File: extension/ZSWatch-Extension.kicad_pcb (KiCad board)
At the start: 4 copper layers, 18 x 18 mm, 37 parts, among them IC501 MAX32664, IC502 LIS2DS12, IC503 MAX86141, IC601 DA7212-01UM2, X701 MB2, X702 MB1, Y501 32kHz

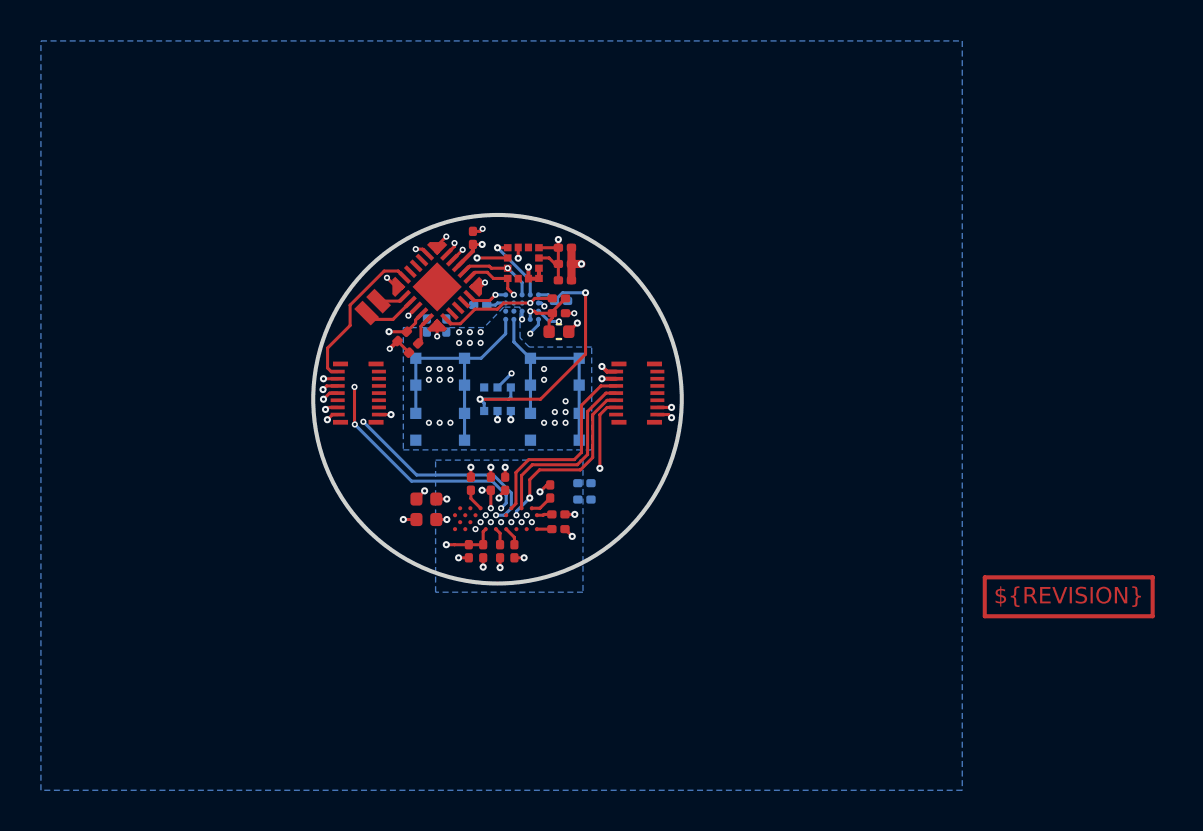
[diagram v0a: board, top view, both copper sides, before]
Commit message: Reduce radius to 8.4 mm
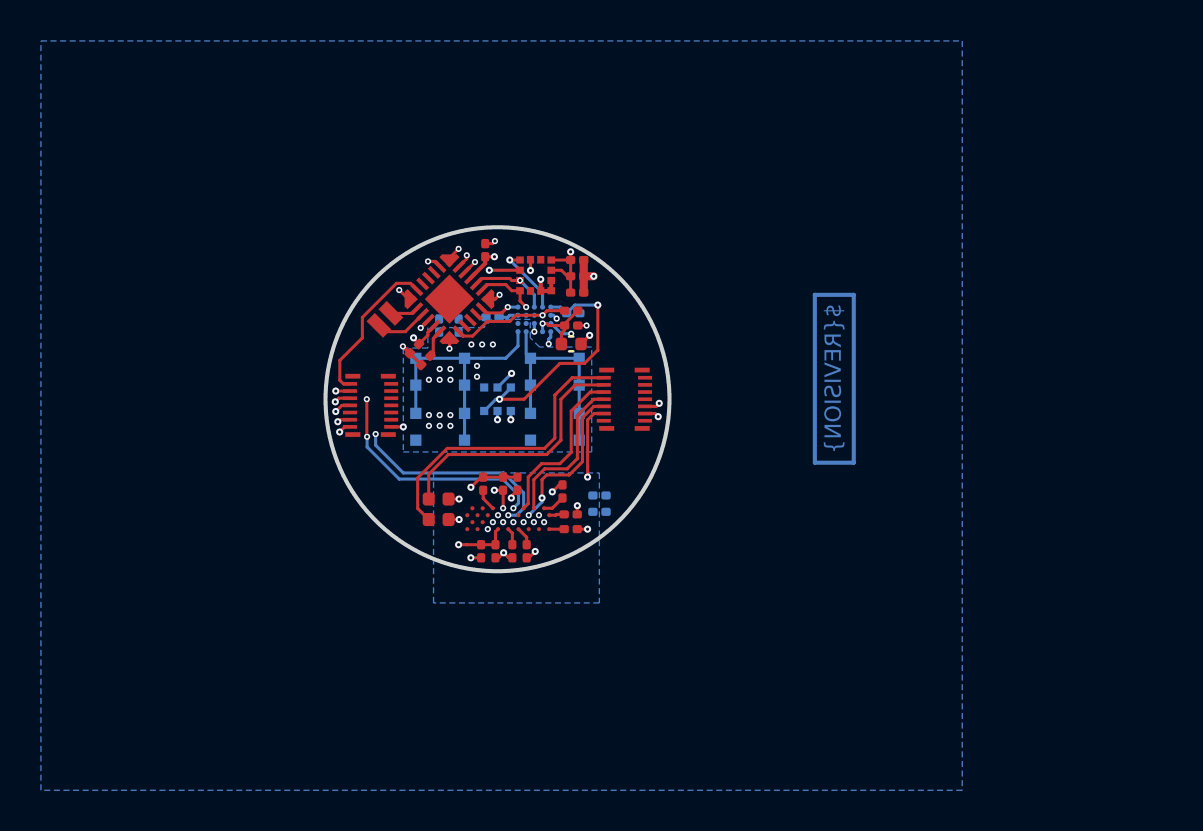
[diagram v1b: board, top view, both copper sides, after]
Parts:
- moved C611 0.95 mm to (210.0, 154.7)
- moved R601 0.95 mm to (210.0, 155.5)
- moved X701 0.85 mm to (198.8, 150.3)
- moved C505 0.85 mm to (208.9, 143.2)
- moved C506 0.85 mm to (208.9, 144.0)
- moved C507 0.85 mm to (208.9, 144.8)
- moved C508 0.85 mm to (208.7, 145.8)
- moved C511 0.85 mm to (208.6, 147.3)
- moved IC502 0.85 mm to (206.9, 143.9)
- moved IC503 0.85 mm to (206.8, 146.1)
- moved R502 0.85 mm to (208.6, 145.7)
- moved C502 0.85 mm to (200.9, 147.5)
- moved C503 0.85 mm to (204.4, 142.7)
- moved C504 0.85 mm to (201.5, 148.1)
- moved C509 0.85 mm to (204.8, 146.0)
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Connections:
- X702 pad 10: unconnected-(X702-Pin_10-Pad10) -> /Project Architecture/Audio/+1V8_PA
- X702 pad 12: /Project Architecture/Audio/+1V8_PA -> GND
- X702 pad 14: GND -> unconnected-(X702-Pin_14-Pad14)
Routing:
- net VSYS: track 35.1 -> 32.2 mm
- net /Project Architecture/Audio/SP-N: track 16.9 -> 14.6 mm, vias 2 -> 0
- net /Project Architecture/Audio/I2S_WCLK: track 9.83 -> 8.22 mm
- net /Project Architecture/Audio/I2S_BCLK: track 9.11 -> 7.67 mm
- net /Project Architecture/Audio/SP-P: track 14.2 -> 12.7 mm, vias 2 -> 0
- net /Project Architecture/Audio/I2S_DIN: track 9.06 -> 7.76 mm
- net /Project Architecture/Audio/I2S_MCLK: track 10.6 -> 9.36 mm
- net GNDA: track 4.33 -> 5.49 mm, vias 12 -> 9
- net Net-(D502-K): track 11.0 -> 9.89 mm
- net Net-(IC503-LED2-DRV): track 7.87 -> 7.06 mm
- net Net-(IC503-LED1-DRV): track 6.33 -> 5.80 mm
- net PD_GND: vias 23 -> 16
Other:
- board size 18 x 18 mm -> 16.8 x 16.8 mm

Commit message: New connector positions
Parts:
- moved X702 1.08 mm to (210.3, 150.6)
- moved X701 0.30 mm to (198.8, 150.0)
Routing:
- net /Project Architecture/Audio/SP-N: track 14.6 -> 12.9 mm
- net /Project Architecture/Audio/I2S_MCLK: track 9.36 -> 7.75 mm
- net /Project Architecture/Audio/SP-P: track 12.7 -> 11.2 mm
- net /Project Architecture/Audio/I2S_DIN: track 7.76 -> 6.18 mm
- net /Project Architecture/Audio/I2S_BCLK: track 7.67 -> 6.11 mm
- net /Project Architecture/Audio/I2S_WCLK: track 8.22 -> 6.70 mm
- net /Project Architecture/Audio/I2C_SCL: track 23.9 -> 23.4 mm
